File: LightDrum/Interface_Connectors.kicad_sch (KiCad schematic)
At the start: 3 parts, among them J1201 0525593652, J1202 0541323662, J1203 PWR-CONN

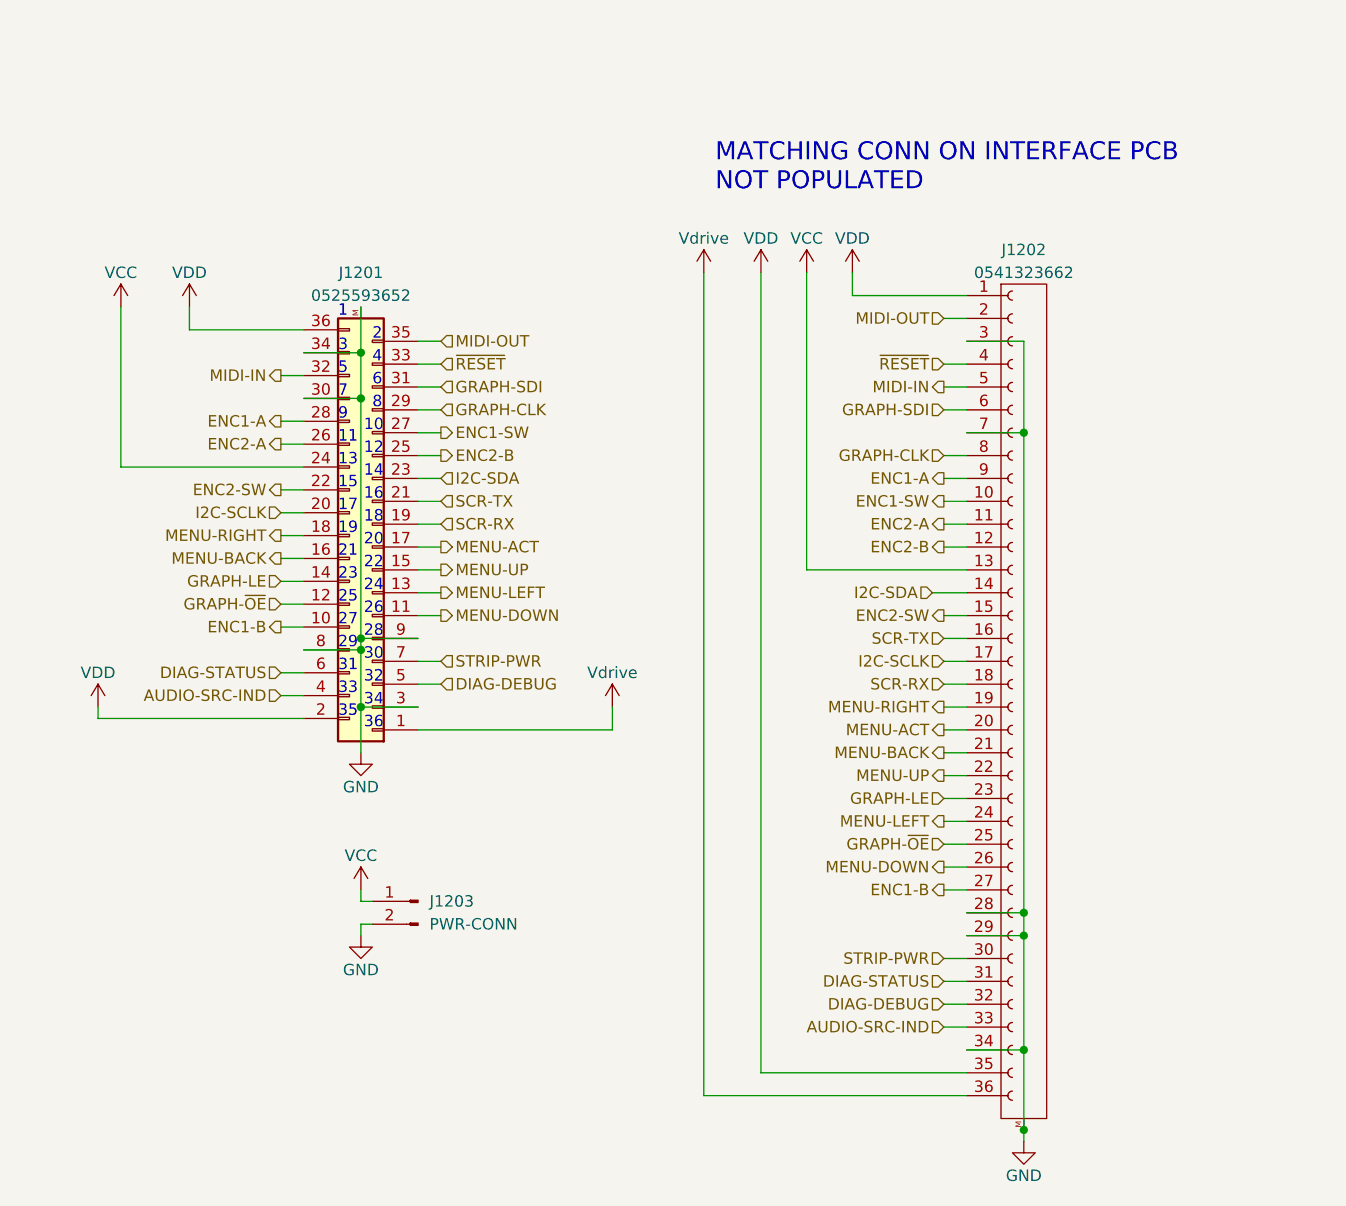
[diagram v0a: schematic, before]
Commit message: Preliminary schematic lock - Starting PCB layout
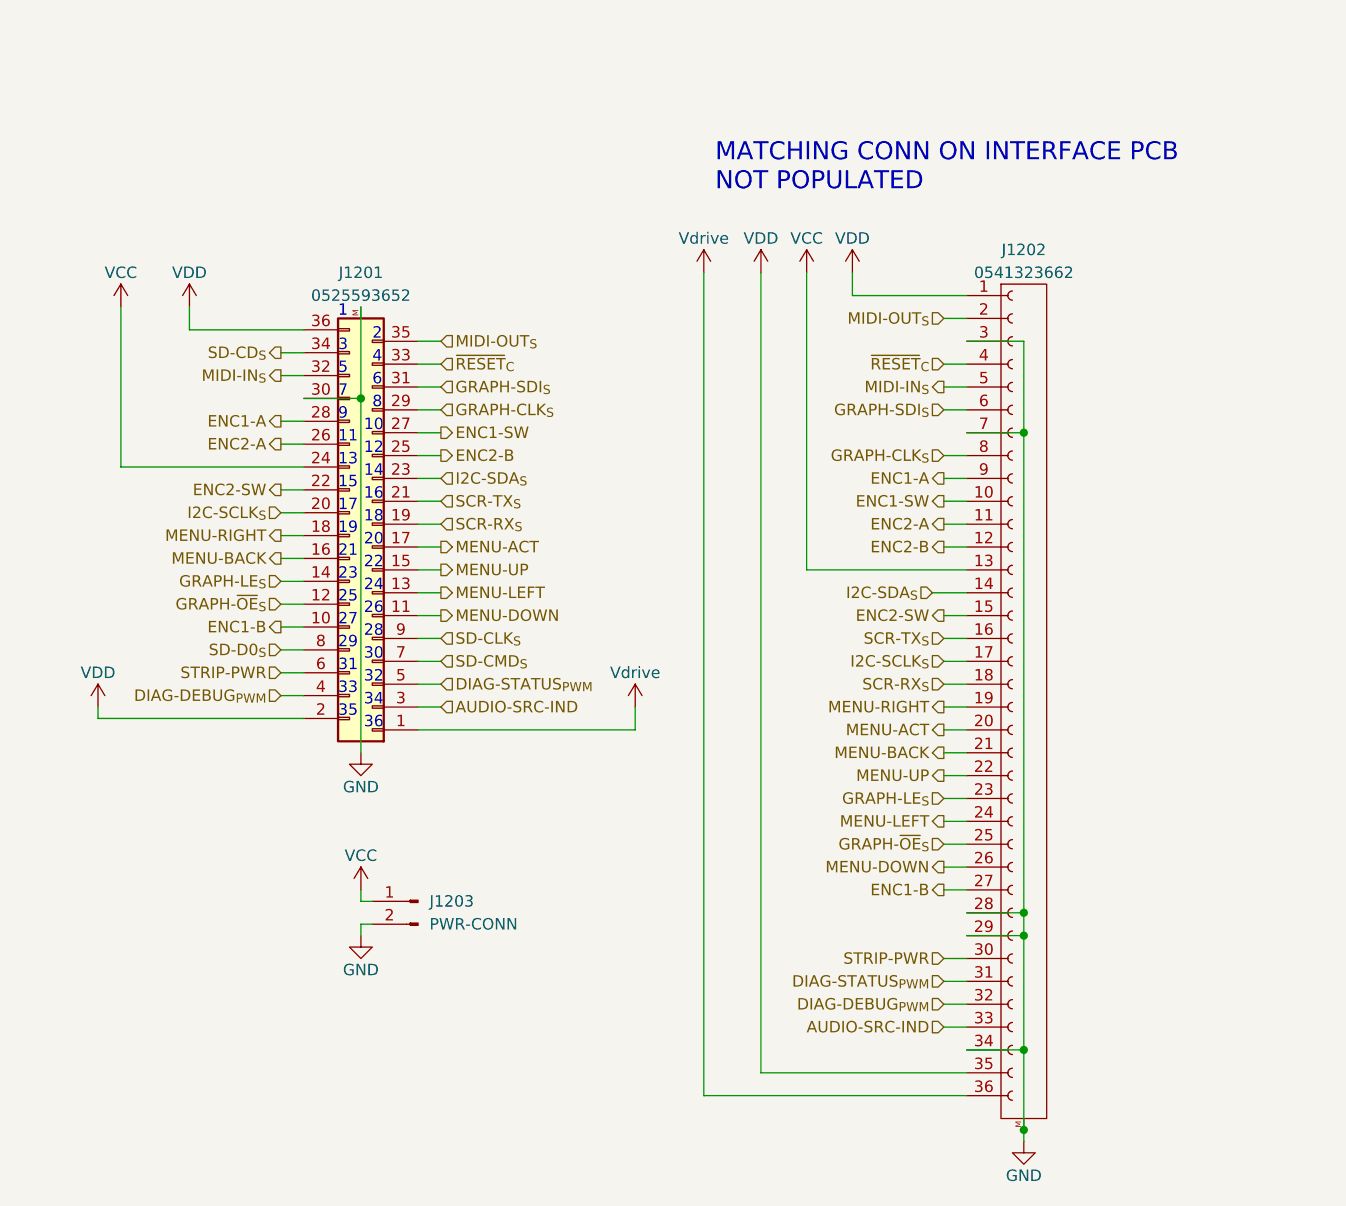
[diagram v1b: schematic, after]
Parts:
- J1201: SupplierPN (none) -> WM7988CT-ND
- J1203: SupplierPN (none) -> 455-2247-ND
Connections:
- net AUDIO-SRC-IND: now also J1201.3 (Pin_3); no longer J1201.4 (Pin_4)
- net GND: no longer J1201.3 (Pin_3), J1201.34 (Pin_34), J1201.8 (Pin_8), J1201.9 (Pin_9)
- net STRIP-PWR: now also J1201.6 (Pin_6); no longer J1201.7 (Pin_7)
- net DIAG-DEBUG renamed DIAG-DEBUG_{PWM}
- net DIAG-DEBUG_{PWM}: now also J1201.4 (Pin_4); no longer J1201.5 (Pin_5)
- net DIAG-STATUS renamed DIAG-STATUS_{PWM}
- net DIAG-STATUS_{PWM}: now also J1201.5 (Pin_5); no longer J1201.6 (Pin_6)
- net GRAPH-CLK renamed GRAPH-CLK_{S}
- net GRAPH-LE renamed GRAPH-LE_{S}
- net GRAPH-SDI renamed GRAPH-SDI_{S}
- net GRAPH-~{OE} renamed GRAPH-~{OE}_{S}
- net I2C-SCLK renamed I2C-SCLK_{S}
- net I2C-SDA renamed I2C-SDA_{S}
- net MIDI-IN renamed MIDI-IN_{S}
- net MIDI-OUT renamed MIDI-OUT_{S}
- net SCR-RX renamed SCR-RX_{S}
- net SCR-TX renamed SCR-TX_{S}
- net ~{RESET} renamed ~{RESET}_{C}
- new net SD-CD_{S}: J1201.34 (Pin_34)
- new net SD-CLK_{S}: J1201.9 (Pin_9)
- new net SD-CMD_{S}: J1201.7 (Pin_7)
- new net SD-D0_{S}: J1201.8 (Pin_8)

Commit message: Component placement complete
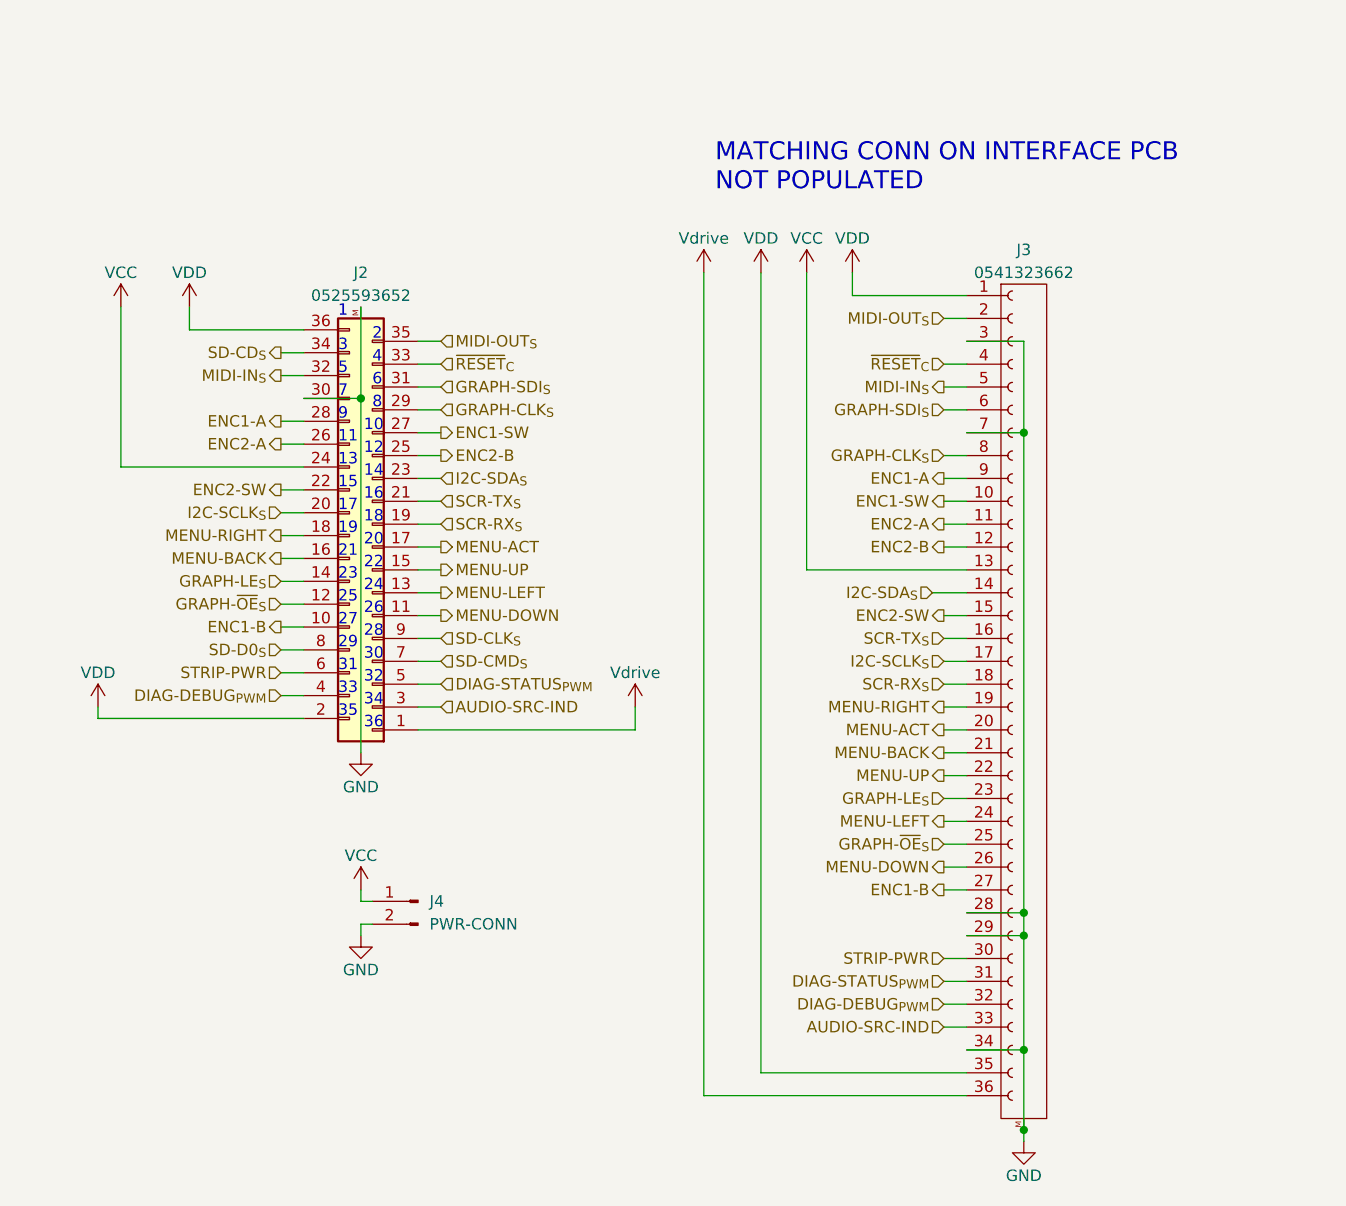
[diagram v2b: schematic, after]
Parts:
- renumbered J1201 to J2, J1202 to J3, J1203 to J4
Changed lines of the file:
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@@
   (symbol (lib_id "power:VDD") (at 31.75 44.45 0) (unit 1)
     (in_bom yes) (on_board yes) (dnp no)
-    (property "Reference" "#PWR0143" (at 31.75 48.26 0)
+    (property "Reference" "#PWR026" (at 31.75 48.26 0)
       (effects (font (size 1.27 1.27)) hide)
     )
@@
       (project "LightDrum"
         (path "/7f137461-fd46-4a4c-8db7-555d487fb3ca/37b1a4e5-7bc5-4d58-948d-cb24160396b1"
-          (reference "#PWR0143") (unit 1)
+          (reference "#PWR026") (unit 1)
         )
       )
@@
   (symbol (lib_id "power:GND") (at 50.8 93.98 0) (unit 1)
     (in_bom yes) (on_board yes) (dnp no)
-    (property "Reference" "#PWR01212" (at 50.8 100.33 0)
+    (property "Reference" "#PWR029" (at 50.8 100.33 0)
       (effects (font (size 1.27 1.27)) hide)
     )
@@
       (project "LightDrum"
         (path "/7f137461-fd46-4a4c-8db7-555d487fb3ca/37b1a4e5-7bc5-4d58-948d-cb24160396b1"
-          (reference "#PWR01212") (unit 1)
+          (reference "#PWR029") (unit 1)
         )
       )
@@
   (symbol (lib_id "Daxxn_Connectors:0541323662") (at 123.19 86.36 0) (unit 1)
     (in_bom no) (on_board no) (dnp no)
-    (property "Reference" "J1202" (at 124.46 38.1 0)
+    (property "Reference" "J3" (at 124.46 38.1 0)
       (effects (font (size 1.27 1.27)))
     )
@@
       (project "LightDrum"
         (path "/7f137461-fd46-4a4c-8db7-555d487fb3ca/37b1a4e5-7bc5-4d58-948d-cb24160396b1"
-          (reference "J1202") (unit 1)
+          (reference "J3") (unit 1)
         )
       )
@@
   (symbol (lib_id "power:GND") (at 124.46 137.16 0) (unit 1)
     (in_bom yes) (on_board yes) (dnp no)
-    (property "Reference" "#PWR01216" (at 124.46 143.51 0)
+    (property "Reference" "#PWR032" (at 124.46 143.51 0)
       (effects (font (size 1.27 1.27)) hide)
     )
@@
       (project "LightDrum"
         (path "/7f137461-fd46-4a4c-8db7-555d487fb3ca/37b1a4e5-7bc5-4d58-948d-cb24160396b1"
-          (reference "#PWR01216") (unit 1)
+          (reference "#PWR032") (unit 1)
         )
       )
@@
   (symbol (lib_id "power:GND") (at 50.8 114.3 0) (unit 1)
     (in_bom yes) (on_board yes) (dnp no)
-    (property "Reference" "#PWR01214" (at 50.8 120.65 0)
+    (property "Reference" "#PWR031" (at 50.8 120.65 0)
       (effects (font (size 1.27 1.27)) hide)
     )
@@
       (project "LightDrum"
         (path "/7f137461-fd46-4a4c-8db7-555d487fb3ca/37b1a4e5-7bc5-4d58-948d-cb24160396b1"
-          (reference "#PWR01214") (unit 1)
+          (reference "#PWR031") (unit 1)
         )
       )
@@
   (symbol (lib_id "power:VCC") (at 100.33 40.64 0) (unit 1)
     (in_bom yes) (on_board yes) (dnp no)
-    (property "Reference" "#PWR0122" (at 100.33 44.45 0)
+    (property "Reference" "#PWR023" (at 100.33 44.45 0)
       (effects (font (size 1.27 1.27)) hide)
     )
@@
       (project "LightDrum"
         (path "/7f137461-fd46-4a4c-8db7-555d487fb3ca/37b1a4e5-7bc5-4d58-948d-cb24160396b1"
-          (reference "#PWR0122") (unit 1)
+          (reference "#PWR023") (unit 1)
         )
       )
@@
   (symbol (lib_id "power:Vdrive") (at 88.9 40.64 0) (unit 1)
     (in_bom yes) (on_board yes) (dnp no)
-    (property "Reference" "#PWR01208" (at 83.82 44.45 0)
+    (property "Reference" "#PWR021" (at 83.82 44.45 0)
       (effects (font (size 1.27 1.27)) hide)
     )
@@
       (project "LightDrum"
         (path "/7f137461-fd46-4a4c-8db7-555d487fb3ca/37b1a4e5-7bc5-4d58-948d-cb24160396b1"
-          (reference "#PWR01208") (unit 1)
+          (reference "#PWR021") (unit 1)
         )
       )
@@
   (symbol (lib_id "power:VDD") (at 95.25 40.64 0) (unit 1)
     (in_bom yes) (on_board yes) (dnp no)
-    (property "Reference" "#PWR01215" (at 95.25 44.45 0)
+    (property "Reference" "#PWR022" (at 95.25 44.45 0)
       (effects (font (size 1.27 1.27)) hide)
     )
@@
       (project "LightDrum"
         (path "/7f137461-fd46-4a4c-8db7-555d487fb3ca/37b1a4e5-7bc5-4d58-948d-cb24160396b1"
-          (reference "#PWR01215") (unit 1)
+          (reference "#PWR022") (unit 1)
         )
       )
@@
   (symbol (lib_id "power:Vdrive") (at 81.28 88.9 0) (unit 1)
     (in_bom yes) (on_board yes) (dnp no)
-    (property "Reference" "#PWR01209" (at 76.2 92.71 0)
+    (property "Reference" "#PWR028" (at 76.2 92.71 0)
       (effects (font (size 1.27 1.27)) hide)
     )
@@
       (project "LightDrum"
         (path "/7f137461-fd46-4a4c-8db7-555d487fb3ca/37b1a4e5-7bc5-4d58-948d-cb24160396b1"
-          (reference "#PWR01209") (unit 1)
+          (reference "#PWR028") (unit 1)
         )
       )
@@
   (symbol (lib_id "power:VCC") (at 24.13 44.45 0) (unit 1)
     (in_bom yes) (on_board yes) (dnp no)
-    (property "Reference" "#PWR0124" (at 24.13 48.26 0)
+    (property "Reference" "#PWR025" (at 24.13 48.26 0)
       (effects (font (size 1.27 1.27)) hide)
     )
@@
       (project "LightDrum"
         (path "/7f137461-fd46-4a4c-8db7-555d487fb3ca/37b1a4e5-7bc5-4d58-948d-cb24160396b1"
-          (reference "#PWR0124") (unit 1)
+          (reference "#PWR025") (unit 1)
         )
       )
@@
   (symbol (lib_id "Connector:Conn_01x02_Male") (at 57.15 110.49 0) (mirror y) (unit 1)
     (in_bom yes) (on_board yes) (dnp no)
-    (property "Reference" "J1203" (at 58.42 110.49 0)
+    (property "Reference" "J4" (at 58.42 110.49 0)
       (effects (font (size 1.27 1.27)) (justify right))
     )
@@
       (project "LightDrum"
         (path "/7f137461-fd46-4a4c-8db7-555d487fb3ca/37b1a4e5-7bc5-4d58-948d-cb24160396b1"
-          (reference "J1203") (unit 1)
+          (reference "J4") (unit 1)
         )
       )
@@
   (symbol (lib_id "power:VDD") (at 21.59 88.9 0) (unit 1)
     (in_bom yes) (on_board yes) (dnp no)
-    (property "Reference" "#PWR01211" (at 21.59 92.71 0)
+    (property "Reference" "#PWR027" (at 21.59 92.71 0)
       (effects (font (size 1.27 1.27)) hide)
     )
@@
       (project "LightDrum"
         (path "/7f137461-fd46-4a4c-8db7-555d487fb3ca/37b1a4e5-7bc5-4d58-948d-cb24160396b1"
-          (reference "#PWR01211") (unit 1)
+          (reference "#PWR027") (unit 1)
         )
       )
@@
   (symbol (lib_id "power:VDD") (at 105.41 40.64 0) (unit 1)
     (in_bom yes) (on_board yes) (dnp no)
-    (property "Reference" "#PWR0123" (at 105.41 44.45 0)
+    (property "Reference" "#PWR024" (at 105.41 44.45 0)
       (effects (font (size 1.27 1.27)) hide)
     )
@@
       (project "LightDrum"
         (path "/7f137461-fd46-4a4c-8db7-555d487fb3ca/37b1a4e5-7bc5-4d58-948d-cb24160396b1"
-          (reference "#PWR0123") (unit 1)
+          (reference "#PWR024") (unit 1)
         )
       )
@@
   (symbol (lib_id "power:VCC") (at 50.8 109.22 0) (unit 1)
     (in_bom yes) (on_board yes) (dnp no)
-    (property "Reference" "#PWR01213" (at 50.8 113.03 0)
+    (property "Reference" "#PWR030" (at 50.8 113.03 0)
       (effects (font (size 1.27 1.27)) hide)
     )
@@
       (project "LightDrum"
         (path "/7f137461-fd46-4a4c-8db7-555d487fb3ca/37b1a4e5-7bc5-4d58-948d-cb24160396b1"
-          (reference "#PWR01213") (unit 1)
+          (reference "#PWR030") (unit 1)
         )
       )
@@
   (symbol (lib_id "Daxxn_Connectors:0525593652") (at 52.07 71.12 180) (unit 1)
     (in_bom yes) (on_board yes) (dnp no)
-    (property "Reference" "J1201" (at 50.8 40.64 0)
+    (property "Reference" "J2" (at 50.8 40.64 0)
       (effects (font (size 1.27 1.27)))
     )
@@
       (project "LightDrum"
         (path "/7f137461-fd46-4a4c-8db7-555d487fb3ca/37b1a4e5-7bc5-4d58-948d-cb24160396b1"
-          (reference "J1201") (unit 1)
-        )
-      )
+          (reference "J2") (unit 1)
+        )
+      )

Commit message: First draft layout almost complete
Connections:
- net ENC1-A: now also J2.21 (Pin_21); no longer J2.28 (Pin_28)
- net ENC1-B: now also J2.14 (Pin_14); no longer J2.10 (Pin_10)
- net ENC2-A: now also J2.23 (Pin_23); no longer J2.26 (Pin_26)
- net ENC2-SW: now also J2.19 (Pin_19); no longer J2.22 (Pin_22)
- net GND: now also J2.32 (Pin_32); no longer J2.30 (Pin_30)
- net GRAPH-CLK_{S}: now also J2.31 (Pin_31); no longer J2.29 (Pin_29)
- net GRAPH-LE_{S}: now also J2.12 (Pin_12); no longer J2.14 (Pin_14)
- net GRAPH-SDI_{S}: now also J2.13 (Pin_13); no longer J2.31 (Pin_31)
- net GRAPH-~{OE}_{S}: now also J2.10 (Pin_10); no longer J2.12 (Pin_12)
- net I2C-SCLK_{S}: now also J2.22 (Pin_22); no longer J2.20 (Pin_20)
- net I2C-SDA_{S}: now also J2.24 (Pin_24); no longer J2.23 (Pin_23)
- net MENU-ACT: no longer J2.17 (Pin_17)
- net MENU-BACK: no longer J2.16 (Pin_16)
- net MENU-DOWN: no longer J2.11 (Pin_11)
- net MENU-LEFT: no longer J2.13 (Pin_13)
- net MENU-RIGHT: no longer J2.18 (Pin_18)
- net MENU-UP: no longer J2.15 (Pin_15)
- net MIDI-IN_{S}: now also J2.34 (Pin_34); no longer J2.32 (Pin_32)
- net SCR-RX_{S}: now also J2.28 (Pin_28); no longer J2.19 (Pin_19)
- net SCR-TX_{S}: now also J2.30 (Pin_30); no longer J2.21 (Pin_21)
- net SD-CD_{S}: now also J2.20 (Pin_20); no longer J2.34 (Pin_34)
- net VCC: now also J2.26 (Pin_26); no longer J2.24 (Pin_24)
- new net MENU-ACT_{INT}: J2.17 (Pin_17)
- new net MENU-BACK_{INT}: J2.16 (Pin_16)
- new net MENU-DOWN_{INT}: J2.11 (Pin_11)
- new net MENU-LEFT_{INT}: J2.29 (Pin_29)
- new net MENU-RIGHT_{INT}: J2.18 (Pin_18)
- new net MENU-UP_{INT}: J2.15 (Pin_15)
